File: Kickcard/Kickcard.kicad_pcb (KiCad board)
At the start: 2 copper layers, 138.7 x 110.2 mm, 25 parts, among them J1 Conn_Side_Expansion, J2 Conn_01x01_Pin, SW1 SW_DIP_x04, SW2 SW_MEC_5E, SW3 SW_MEC_5E, U1 GAL20B8, U2 SST39SF040, U3 SST39SF040, U4 27C400

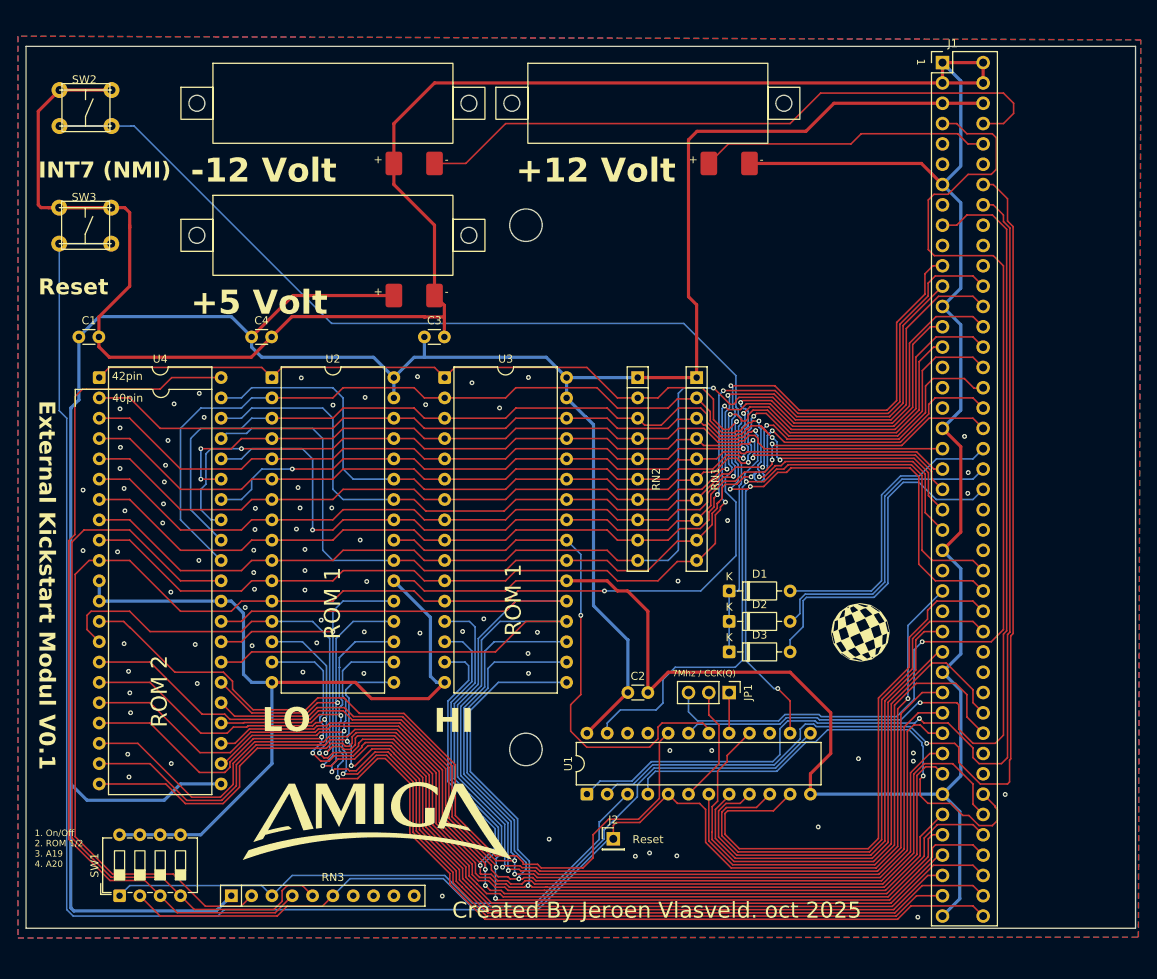
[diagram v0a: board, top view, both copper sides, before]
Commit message: added gal logic
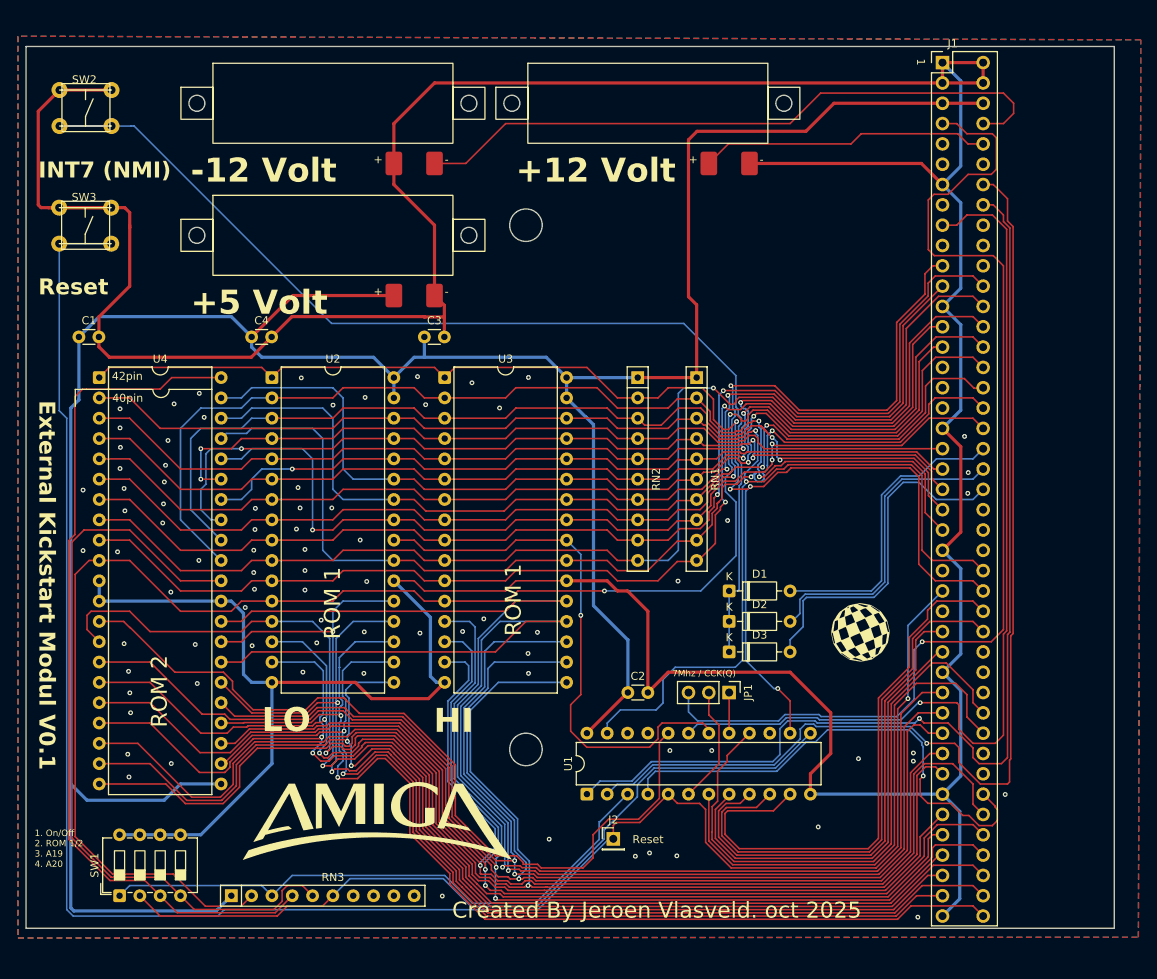
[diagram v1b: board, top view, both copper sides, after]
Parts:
- U1: value GAL20B8 -> PAL20L8
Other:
- board size 138.7 x 110.2 mm -> 136 x 110.2 mm
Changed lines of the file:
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@@
 			)
 		)
-		(property "Value" "GAL20B8"
+		(property "Value" "PAL20L8"
 			(at 3.81 30.27 90)
 			(layer "F.Fab")
@@
 		(fp_line
 			(start -1.775 108)
-			(end 24.13 108)
+			(end 21.59 108)
 			(stroke
 				(width 0.05)
@@
 		)
 		(fp_line
-			(start 24.13 -1.778)
+			(start 21.59 -1.778)
 			(end -1.77 -1.77)
 			(stroke
@@
 		)
 		(fp_line
-			(start 24.13 108)
-			(end 24.13 -1.778)
+			(start 21.59 108)
+			(end 21.59 -1.778)
 			(stroke
 				(width 0.05)
@@
 	)
 	(gr_rect
-		(start 75.4272 39.0252)
-		(end 214.1112 149.2612)
+		(start 75.4272 39.0398)
+		(end 211.455 149.2612)
 		(stroke
 			(width 0.05)

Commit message: added test points
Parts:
- removed J2: Conn_01x01_Pin, Connector_PinHeader_2.54mm:PinHeader_1x01_P2.54mm_Vertical
- added 7Mhz1: Conn_01x01, TestPoint:TestPoint_Pad_D1.0mm, F.Cu at (141.0, 135.2)
- added A1: Conn_01x01, TestPoint:TestPoint_Pad_D1.0mm, F.Cu at (146.1, 61.0)
- added A10: Conn_01x01, TestPoint:TestPoint_Pad_D1.0mm, F.Cu at (148.6, 64.8)
- added A11: Conn_01x01, TestPoint:TestPoint_Pad_D1.0mm, F.Cu at (151.1, 64.8)
- added A12: Conn_01x01, TestPoint:TestPoint_Pad_D1.0mm, F.Cu at (153.7, 64.8)
- added A13: Conn_01x01, TestPoint:TestPoint_Pad_D1.0mm, F.Cu at (156.2, 64.8)
- added A14: Conn_01x01, TestPoint:TestPoint_Pad_D1.0mm, F.Cu at (158.8, 64.8)
- added A15: Conn_01x01, TestPoint:TestPoint_Pad_D1.0mm, F.Cu at (161.3, 64.8)
- added A16: Conn_01x01, TestPoint:TestPoint_Pad_D1.0mm, F.Cu at (163.8, 64.8)
- added A17: Conn_01x01, TestPoint:TestPoint_Pad_D1.0mm, F.Cu at (146.1, 68.6)
- added A18: Conn_01x01, TestPoint:TestPoint_Pad_D1.0mm, F.Cu at (148.6, 68.6)
- added A19: Conn_01x01, TestPoint:TestPoint_Pad_D1.0mm, F.Cu at (151.1, 68.6)
- added A2: Conn_01x01, TestPoint:TestPoint_Pad_D1.0mm, F.Cu at (148.6, 61.0)
- added A20: Conn_01x01, TestPoint:TestPoint_Pad_D1.0mm, F.Cu at (153.7, 68.6)
- added A21: Conn_01x01, TestPoint:TestPoint_Pad_D1.0mm, F.Cu at (156.2, 68.6)
- added A22: Conn_01x01, TestPoint:TestPoint_Pad_D1.0mm, F.Cu at (158.8, 68.6)
- added A23: Conn_01x01, TestPoint:TestPoint_Pad_D1.0mm, F.Cu at (161.3, 68.6)
- added A3: Conn_01x01, TestPoint:TestPoint_Pad_D1.0mm, F.Cu at (151.1, 61.0)
- added A4: Conn_01x01, TestPoint:TestPoint_Pad_D1.0mm, F.Cu at (153.7, 61.0)
- added A5: Conn_01x01, TestPoint:TestPoint_Pad_D1.0mm, F.Cu at (156.2, 61.0)
- added A6: Conn_01x01, TestPoint:TestPoint_Pad_D1.0mm, F.Cu at (158.8, 61.0)
- added A7: Conn_01x01, TestPoint:TestPoint_Pad_D1.0mm, F.Cu at (161.3, 61.0)
- added A8: Conn_01x01, TestPoint:TestPoint_Pad_D1.0mm, F.Cu at (163.8, 61.0)
- added A9: Conn_01x01, TestPoint:TestPoint_Pad_D1.0mm, F.Cu at (146.1, 64.8)
- added AS: Conn_01x01, TestPoint:TestPoint_Pad_D1.0mm, F.Cu at (135.9, 132.1)
- added CCK: Conn_01x01, TestPoint:TestPoint_Pad_D1.0mm, F.Cu at (133.3, 135.2)
- added CCKQ: Conn_01x01, TestPoint:TestPoint_Pad_D1.0mm, F.Cu at (130.8, 135.2)
- added Clk_in: Conn_01x01, TestPoint:TestPoint_Pad_D1.0mm, F.Cu at (137.2, 135.2)
- added D0: Conn_01x01, TestPoint:TestPoint_Pad_D1.0mm, F.Cu at (103.4, 136.3)
- added D1: Conn_01x01, TestPoint:TestPoint_Pad_D1.0mm, F.Cu at (105.9, 136.3)
- added D10: Conn_01x01, TestPoint:TestPoint_Pad_D1.0mm, F.Cu at (108.5, 140.1)
- added D11: Conn_01x01, TestPoint:TestPoint_Pad_D1.0mm, F.Cu at (111.0, 140.1)
- added D12: Conn_01x01, TestPoint:TestPoint_Pad_D1.0mm, F.Cu at (113.5, 140.1)
- added D13: Conn_01x01, TestPoint:TestPoint_Pad_D1.0mm, F.Cu at (116.1, 140.1)
- added D14: Conn_01x01, TestPoint:TestPoint_Pad_D1.0mm, F.Cu at (118.6, 140.1)
- added D15: Conn_01x01, TestPoint:TestPoint_Pad_D1.0mm, F.Cu at (121.2, 140.1)
- added D2: Conn_01x01, TestPoint:TestPoint_Pad_D1.0mm, F.Cu at (108.5, 136.3)
- added D3: Conn_01x01, TestPoint:TestPoint_Pad_D1.0mm, F.Cu at (111.0, 136.3)
- added D4: Conn_01x01, TestPoint:TestPoint_Pad_D1.0mm, F.Cu at (113.5, 136.3)
- added D5: Conn_01x01, TestPoint:TestPoint_Pad_D1.0mm, F.Cu at (116.1, 136.3)
- added D6: Conn_01x01, TestPoint:TestPoint_Pad_D1.0mm, F.Cu at (118.6, 136.3)
- added D7: Conn_01x01, TestPoint:TestPoint_Pad_D1.0mm, F.Cu at (121.2, 136.3)
- added D8: Conn_01x01, TestPoint:TestPoint_Pad_D1.0mm, F.Cu at (103.4, 140.1)
- added D9: Conn_01x01, TestPoint:TestPoint_Pad_D1.0mm, F.Cu at (105.9, 140.1)
- added DTACK1: Conn_01x01, TestPoint:TestPoint_Pad_D1.0mm, F.Cu at (137.2, 123.2)
- added LDS: Conn_01x01, TestPoint:TestPoint_Pad_D1.0mm, F.Cu at (130.8, 132.1)
- added R/W1: Conn_01x01, TestPoint:TestPoint_Pad_D1.0mm, F.Cu at (133.3, 123.2)
- added UDS: Conn_01x01, TestPoint:TestPoint_Pad_D1.0mm, F.Cu at (133.3, 132.1)
- moved G*** 38.0 mm to (156.8, 141.6)
- renumbered D1 to DI1, D2 to DI2, D3 to DI3
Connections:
- J1 pad 70: unconnected-(J1-_LDS-Pad70) -> LDS
- J1 pad 72: unconnected-(J1-_UDS-Pad72) -> UDS
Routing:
- net LDS: track 0.00 -> 103.7 mm, vias 0 -> 1
- net UDS: track 0.00 -> 102.5 mm, vias 0 -> 1
- net A20: track 71.2 -> 167.1 mm, vias 0 -> 2
- net A21: track 68.3 -> 159.8 mm, vias 0 -> 2
- net A22: track 61.0 -> 146.8 mm, vias 0 -> 2
- net A23: track 56.6 -> 140.3 mm, vias 0 -> 2
- net D15: track 163.8 -> 208.5 mm, vias 1 -> 2
- net A12: track 116.0 -> 160.2 mm, vias 3 -> 4
- net A13: track 104.3 -> 145.5 mm, vias 2 -> 3
- net CLK_IN: track 14.8 -> 55.7 mm
- net A14: track 96.6 -> 135.2 mm, vias 1 -> 2
- net D14: track 161.2 -> 199.2 mm, vias 1 -> 2
- net A10: track 120.9 -> 158.4 mm, vias 2 -> 3
- net AS: track 61.7 -> 98.0 mm
- net R/W: track 65.2 -> 101.2 mm, vias 0 -> 1
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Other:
- board size 136 x 110.2 mm -> 135.3 x 114.8 mm

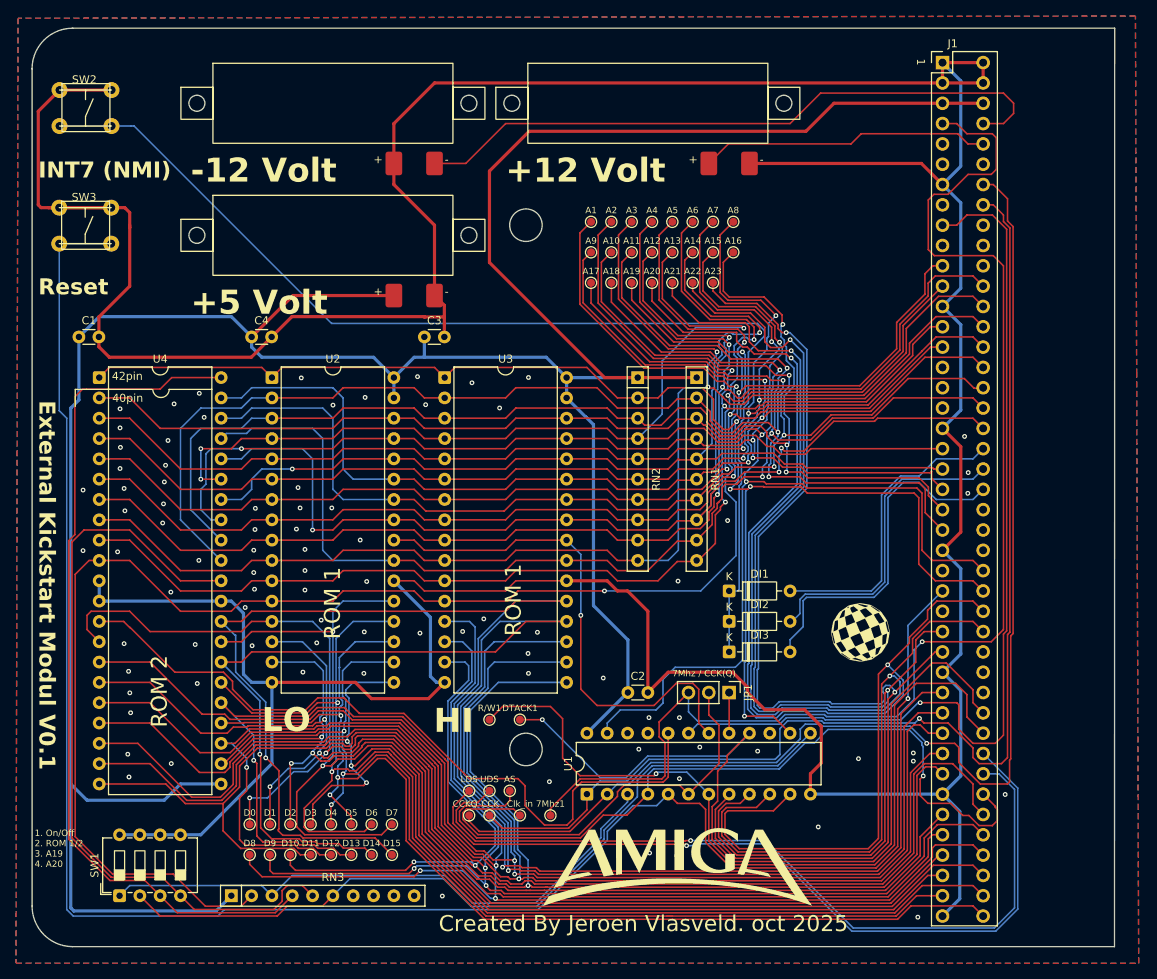
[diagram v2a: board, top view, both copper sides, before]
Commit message: added GND pads
added GND pads to hook oscilloscope GND line
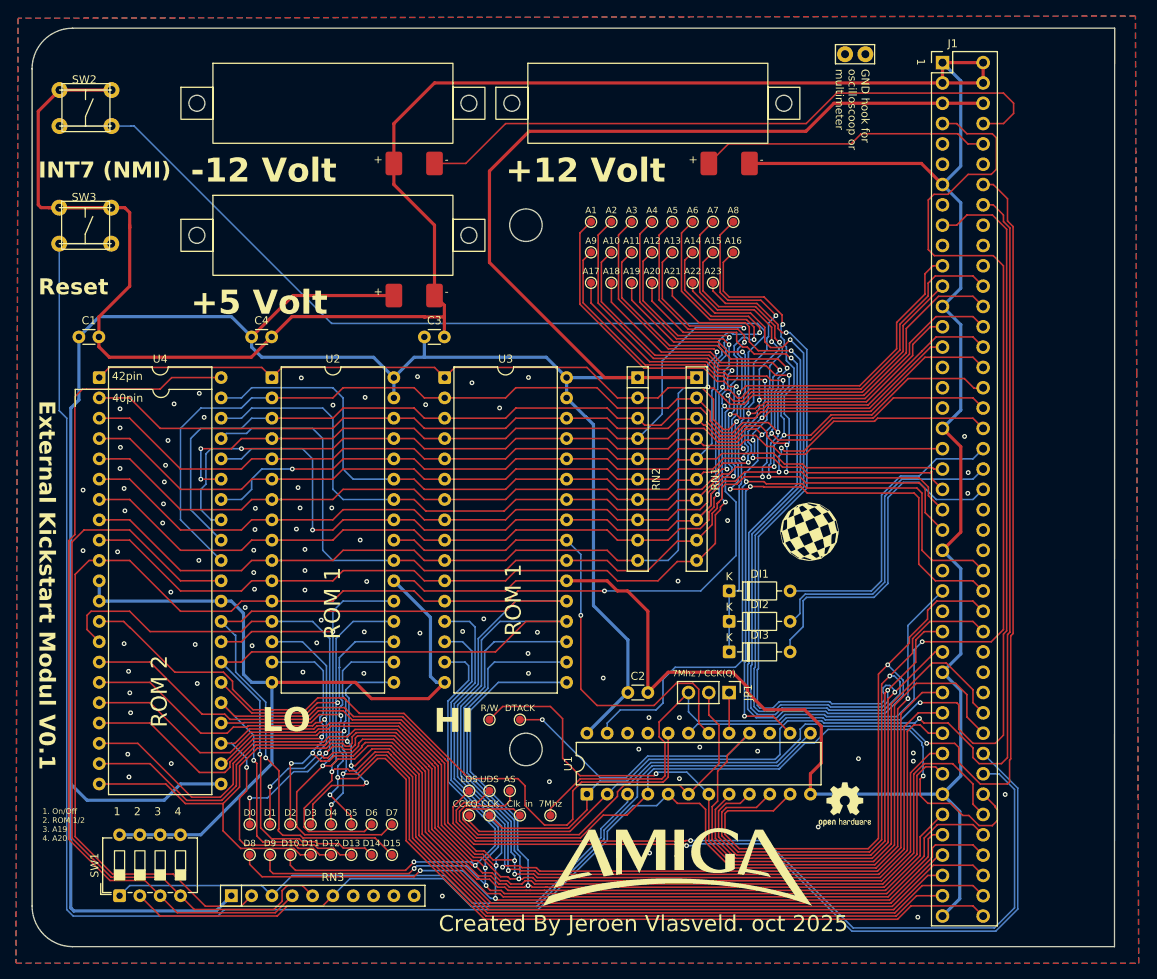
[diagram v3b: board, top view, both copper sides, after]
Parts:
- added REF**: TestPoint_Bridge_Pitch2.54mm_Drill1.0mm, TestPoint:TestPoint_Bridge_Pitch2.54mm_Drill1.0mm, F.Cu at (177.8, 40.0)
- added REF**: OSHW-Logo2_7.3x6mm_SilkScreen, Symbol:OSHW-Logo2_7.3x6mm_SilkScreen, F.Cu at (177.8, 133.8)
- moved G*** 14.1 mm to (173.4, 99.7)
- renumbered 7Mhz1 to 7Mhz, DTACK1 to DTACK, R/W1 to R/W
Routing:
- net D4: track 135.2 -> 134.5 mm
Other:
- board text added: "1"
- board text added: "2"
- board text added: "3"
- board text added: "4"
- board text added: "GND hook for oscilloscoop or multimeter"
- board text added: "dip switch: 1. On/Off 2. ROM 1/2 3. A19 4. A20"
